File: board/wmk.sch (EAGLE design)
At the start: 21 parts, among them IC1 LM1117MPX-3.3, U1 STM32F10XRXT6, X1 PN87520-S

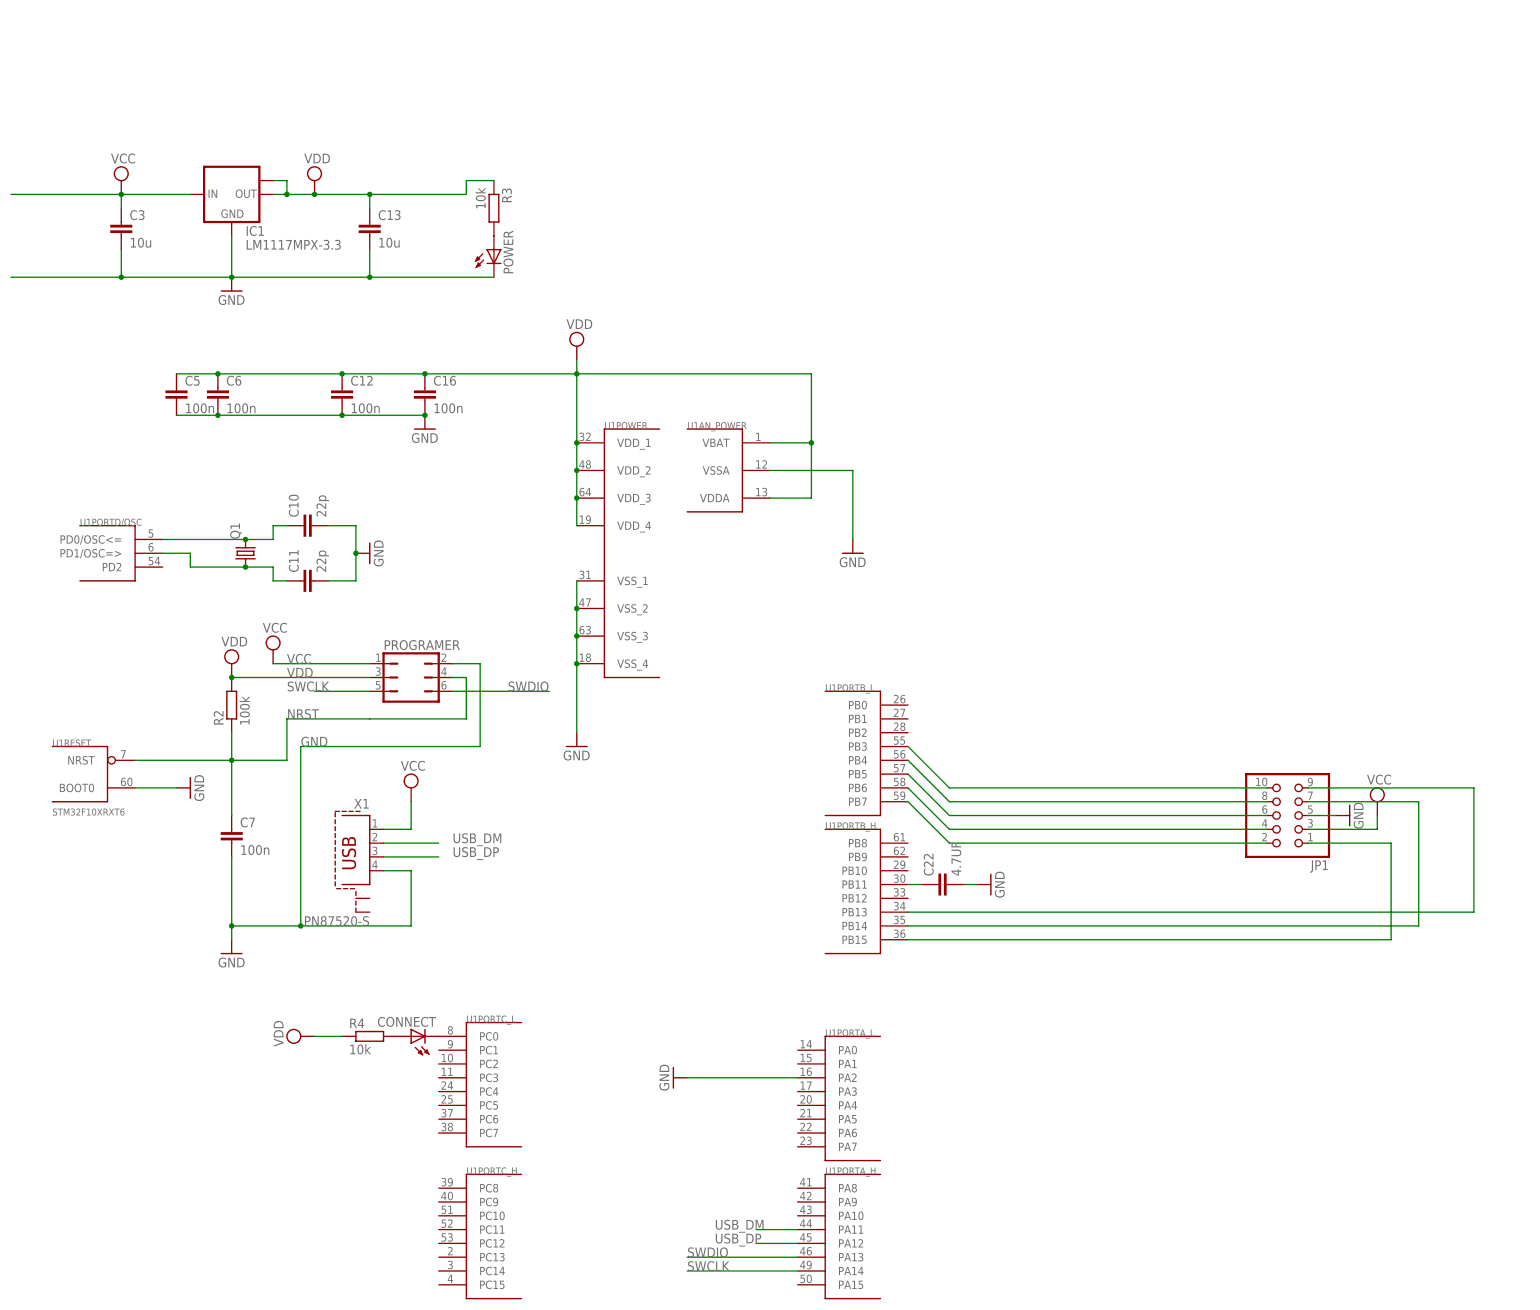
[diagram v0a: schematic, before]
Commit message: Dropping dependency on stm32cubeide, new makefile.
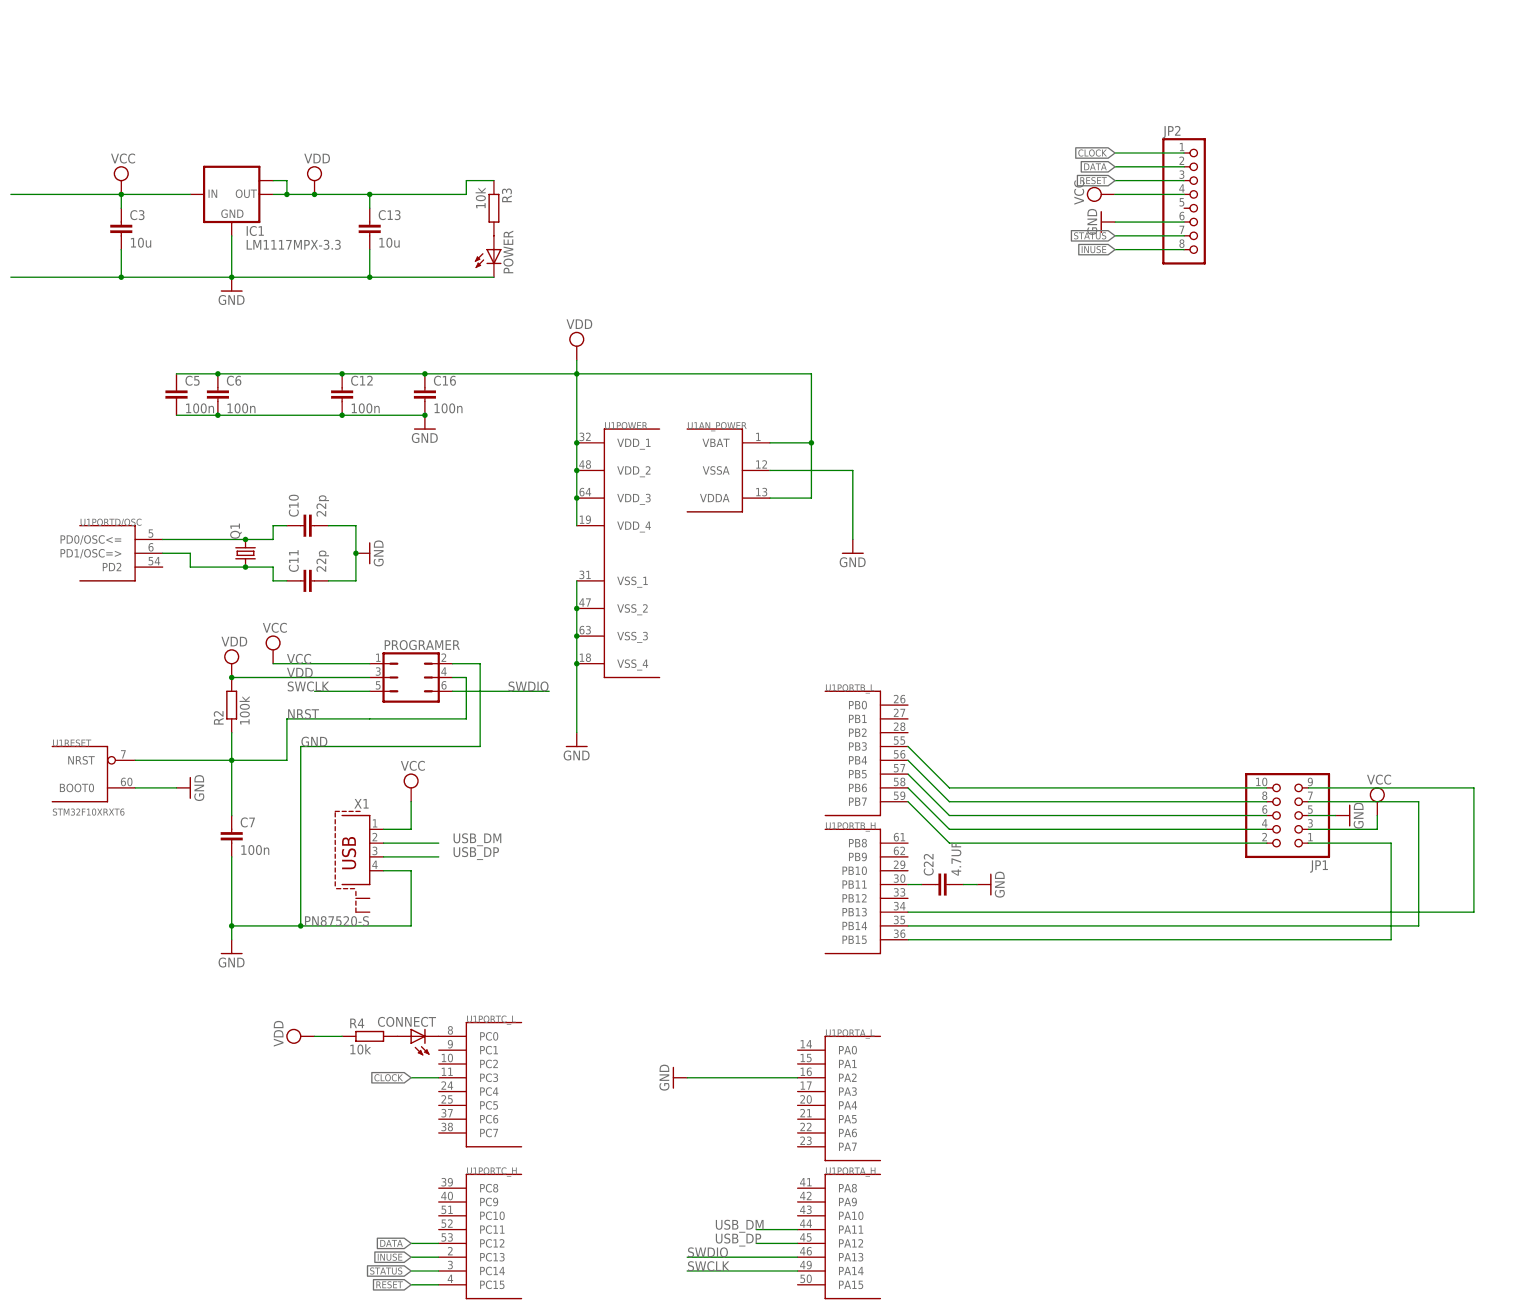
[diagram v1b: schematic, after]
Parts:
- added JP2: (no value), pinhead:PINHD-1X8
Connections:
- new net CLOCK: JP2.1, U1PORTC_L.PC3
- new net DATA: JP2.2, U1PORTC_H.PC12
- new net INUSE: JP2.8, U1PORTC_H.PC13
- new net RESET: JP2.3, U1PORTC_H.PC15
- new net STATUS: JP2.7, U1PORTC_H.PC14
- net GND: now also JP2.6
- net VCC: now also JP2.4
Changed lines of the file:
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@@
 <part name="GND11" library="supply1" deviceset="GND" device=""/>
 <part name="C22" library="rcl" deviceset="C-EU" device="C1206" value="4.7UF"/>
+<part name="JP2" library="pinhead" deviceset="PINHD-1X8" device=""/>
+<part name="GND7" library="supply1" deviceset="GND" device=""/>
+<part name="SUPPLY9" library="supply2" deviceset="VCC" device=""/>
 </parts>
 <sheets>
@@
 <attribute name="NAME" x="-15.621" y="9.144" size="1.778" layer="95" rot="R90"/>
 <attribute name="VALUE" x="-10.541" y="9.144" size="1.778" layer="96" rot="R90"/>
+</instance>
+<instance part="JP2" gate="A" x="33.02" y="132.08"/>
+<instance part="GND7" gate="1" x="15.24" y="129.54" rot="R270">
+<attribute name="VALUE" x="12.7" y="132.08" size="1.778" layer="96" rot="R270"/>
+</instance>
+<instance part="SUPPLY9" gate="G$1" x="15.24" y="134.62" rot="R90">
+<attribute name="VALUE" x="12.065" y="132.715" size="1.778" layer="96" rot="R90"/>
 </instance>
 </instances>
@@
 <pinref part="GND11" gate="1" pin="GND"/>
 <wire x1="-10.16" y1="7.62" x2="-7.62" y2="7.62" width="0.1524" layer="91"/>
+</segment>
+<segment>
+<pinref part="JP2" gate="A" pin="6"/>
+<wire x1="30.48" y1="129.54" x2="17.78" y2="129.54" width="0.1524" layer="91"/>
+<pinref part="GND7" gate="1" pin="GND"/>
 </segment>
 </net>
@@
 <pinref part="SUPPLY13" gate="G$1" pin="VCC"/>
 </segment>
+<segment>
+<pinref part="JP2" gate="A" pin="4"/>
+<wire x1="30.48" y1="134.62" x2="17.78" y2="134.62" width="0.1524" layer="91"/>
+<pinref part="SUPPLY9" gate="G$1" pin="VCC"/>
+</segment>
 </net>
 <net name="SWDIO" class="0">
@@
 </segment>
 </net>
+<net name="CLOCK" class="0">
+<segment>
+<pinref part="JP2" gate="A" pin="1"/>
+<wire x1="30.48" y1="142.24" x2="17.78" y2="142.24" width="0.1524" layer="91"/>
+<label x="17.78" y="142.24" size="1.27" layer="95" rot="R180" xref="yes"/>
+</segment>
+<segment>
+<pinref part="U1" gate="PORTC_L" pin="PC3"/>
+<wire x1="-106.68" y1="-27.94" x2="-111.76" y2="-27.94" width="0.1524" layer="91"/>
+<label x="-111.76" y="-27.94" size="1.27" layer="95" rot="R180" xref="yes"/>
+</segment>
+</net>
+<net name="DATA" class="0">
+<segment>
+<pinref part="JP2" gate="A" pin="2"/>
+<wire x1="30.48" y1="139.7" x2="17.78" y2="139.7" width="0.1524" layer="91"/>
+<label x="17.78" y="139.7" size="1.27" layer="95" rot="R180" xref="yes"/>
+</segment>
+<segment>
+<pinref part="U1" gate="PORTC_H" pin="PC12"/>
+<wire x1="-106.68" y1="-58.42" x2="-111.76" y2="-58.42" width="0.1524" layer="91"/>
+<label x="-111.76" y="-58.42" size="1.27" layer="95" rot="R180" xref="yes"/>
+</segment>
+</net>
+<net name="RESET" class="0">
+<segment>
+<pinref part="JP2" gate="A" pin="3"/>
+<wire x1="30.48" y1="137.16" x2="17.78" y2="137.16" width="0.1524" layer="91"/>
+<label x="17.78" y="137.16" size="1.27" layer="95" rot="R180" xref="yes"/>
+</segment>
+<segment>
+<pinref part="U1" gate="PORTC_H" pin="PC15"/>
+<wire x1="-106.68" y1="-66.04" x2="-111.76" y2="-66.04" width="0.1524" layer="91"/>
+<label x="-111.76" y="-66.04" size="1.27" layer="95" rot="R180" xref="yes"/>
+</segment>
+</net>
+<net name="STATUS" class="0">
+<segment>
+<pinref part="JP2" gate="A" pin="7"/>
+<wire x1="30.48" y1="127" x2="17.78" y2="127" width="0.1524" layer="91"/>
+<label x="17.78" y="127" size="1.27" layer="95" rot="R180" xref="yes"/>
+</segment>
+<segment>
+<pinref part="U1" gate="PORTC_H" pin="PC14"/>
+<wire x1="-106.68" y1="-63.5" x2="-111.76" y2="-63.5" width="0.1524" layer="91"/>
+<label x="-111.76" y="-63.5" size="1.27" layer="95" rot="R180" xref="yes"/>
+</segment>
+</net>
+<net name="INUSE" class="0">
+<segment>
+<pinref part="JP2" gate="A" pin="8"/>
+<wire x1="30.48" y1="124.46" x2="17.78" y2="124.46" width="0.1524" layer="91"/>
+<label x="17.78" y="124.46" size="1.27" layer="95" rot="R180" xref="yes"/>
+</segment>
+<segment>
+<pinref part="U1" gate="PORTC_H" pin="PC13"/>
+<wire x1="-106.68" y1="-60.96" x2="-111.76" y2="-60.96" width="0.1524" layer="91"/>
+<label x="-111.76" y="-60.96" size="1.27" layer="95" rot="R180" xref="yes"/>
+</segment>
+</net>

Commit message: First pass of the CH32 proto. unchecked and untested.
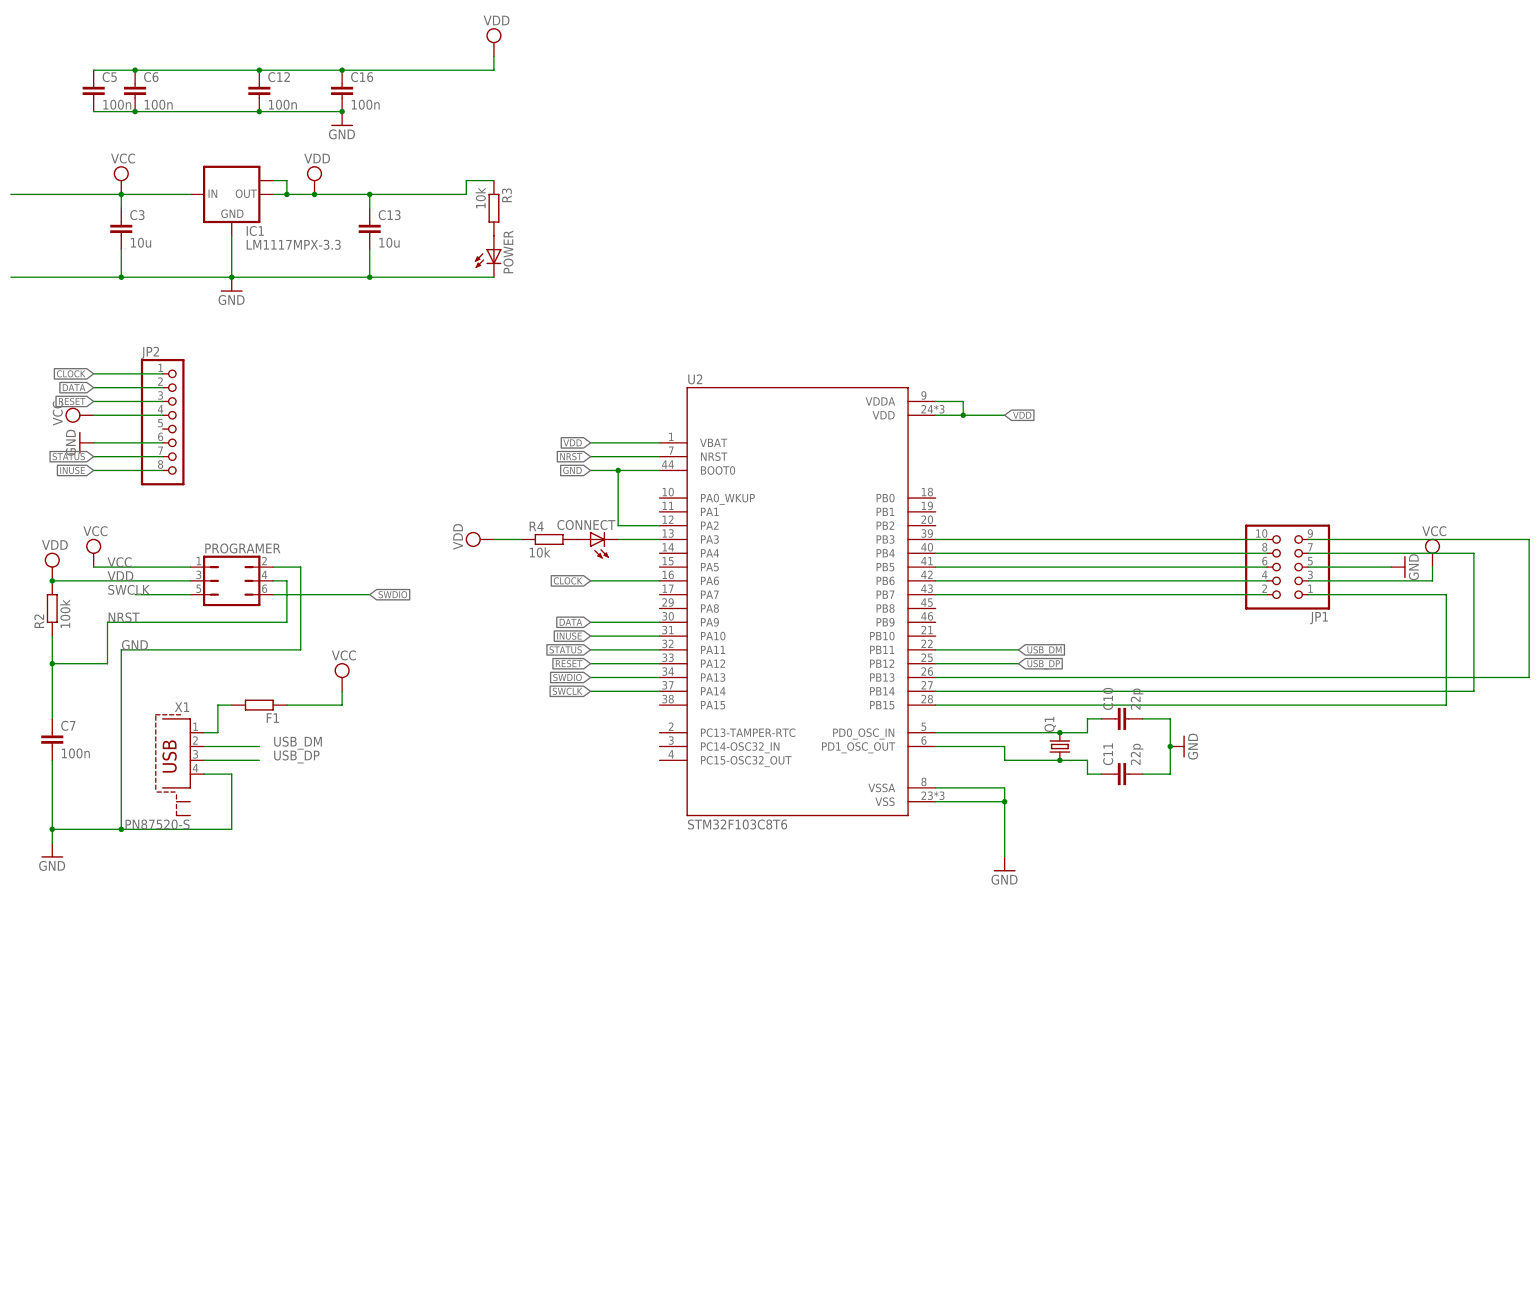
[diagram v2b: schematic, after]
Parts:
- removed C22: 4.7UF, rcl:C-EUC1206
- removed U1: STM32F10XRXT6, stm32:STM32F10XRXT6
- added F1: (no value), eagle-ltspice:RR1206
- added U2: STM32F103C8T6, STM32F103C8T6:STM32F103C8T6
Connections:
- net CLOCK: now also U2.PA6; no longer U1PORTC_L.PC3
- net DATA: now also U2.PA9; no longer U1PORTC_H.PC12
- net GND: now also U2.BOOT0, U2.PA2, U2.VSS, U2.VSSA; no longer C22.2, U1AN_POWER.VSSA, U1PORTA_L.PA2, U1POWER.VSS_1, U1POWER.VSS_2, U1POWER.VSS_3, U1POWER.VSS_4, U1RESET.BOOT0
- net INUSE: now also U2.PA10; no longer U1PORTC_H.PC13
- net N$1: now also U2.PD0_OSC_IN; no longer U1PORTD/OSC.PD0/OSC<=
- net N$10: now also U2.PB6; no longer U1PORTB_L.PB6
- net N$11: now also U2.PB7; no longer U1PORTB_L.PB7
- net N$13: now also U2.PB14; no longer U1PORTB_H.PB14
- net N$15: now also U2.PB13; no longer U1PORTB_H.PB13
- net N$2: now also U2.PD1_OSC_OUT; no longer U1PORTD/OSC.PD1/OSC=>
- net N$3: now also U2.PA3; no longer U1PORTC_L.PC0
- net N$36: now also U2.PB15; no longer U1PORTB_H.PB15
- net N$4: now also F1.2, X1.1; no longer C22.1, U1PORTB_H.PB11
- net N$6: now also U2.PB3; no longer U1PORTB_L.PB3
- net N$8: now also U2.PB4; no longer U1PORTB_L.PB4
- net N$9: now also U2.PB5; no longer U1PORTB_L.PB5
- net NRST: now also U2.NRST; no longer U1RESET.NRST
- net RESET: now also U2.PA12; no longer U1PORTC_H.PC15
- net STATUS: now also U2.PA11; no longer U1PORTC_H.PC14
- net SWCLK: now also U2.PA14; no longer U1PORTA_H.PA14
- net SWDIO: now also U2.PA13; no longer U1PORTA_H.PA13
- net USB_DM: now also U2.PB11; no longer U1PORTA_H.PA11
- net USB_DP: now also U2.PB12; no longer U1PORTA_H.PA12
- net VCC: now also F1.1; no longer X1.1
- net VDD: now also U2.VBAT, U2.VDD, U2.VDDA; no longer U1AN_POWER.VBAT, U1AN_POWER.VDDA, U1POWER.VDD_1, U1POWER.VDD_2, U1POWER.VDD_3, U1POWER.VDD_4
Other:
- moved on the sheet: C10, C11, C12, C16, C5, C6, C7, CONNECT, JP1, JP2, PROGRAMER, Q1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
